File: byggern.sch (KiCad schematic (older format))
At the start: 15 parts, among them U1 ATmega162-16PU

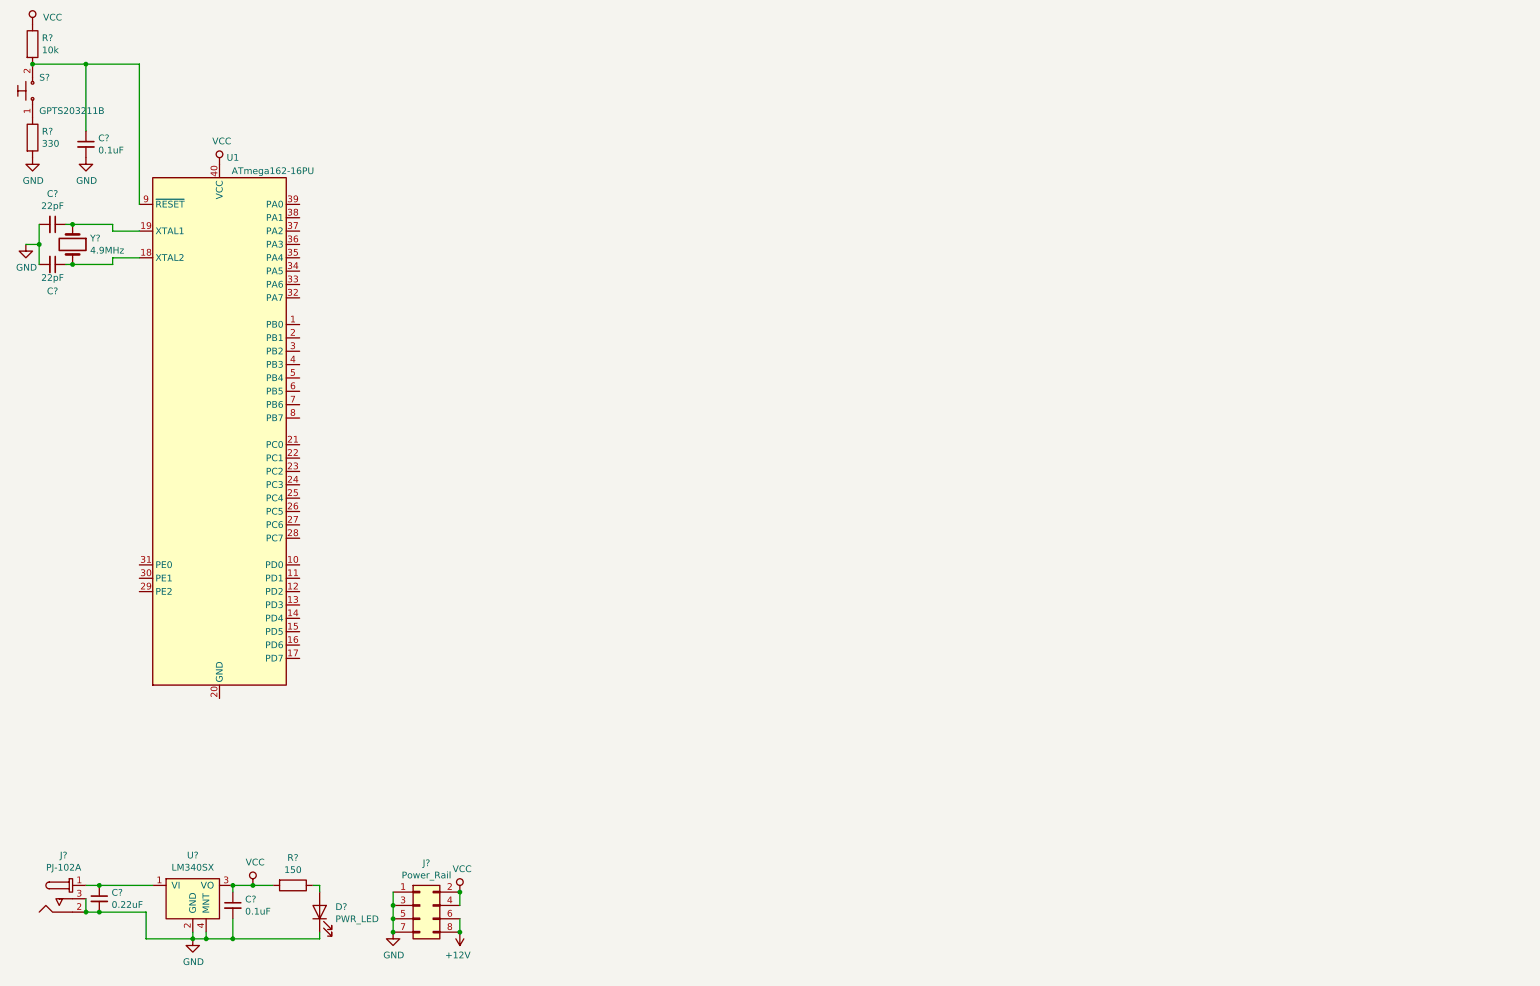
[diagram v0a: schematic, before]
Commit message: Update schematic with usart interface
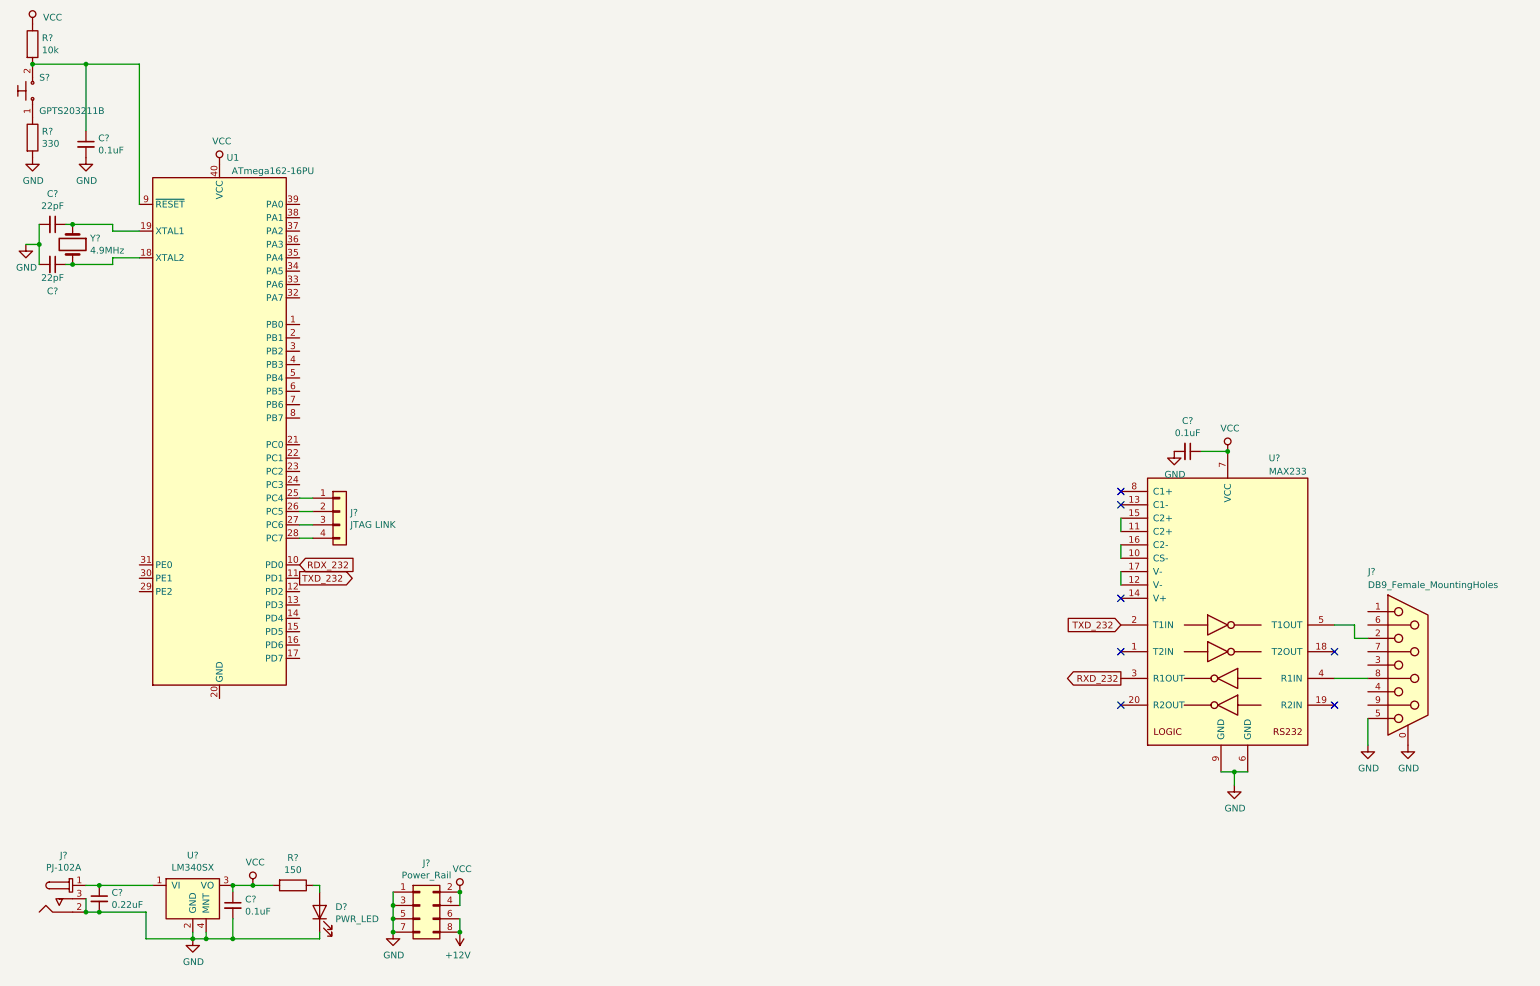
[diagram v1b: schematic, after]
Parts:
- added C?: 0.1uF, symbol Device:C_Small
- added J?: JTAG LINK, symbol Connector_Generic:Conn_01x04
- added J?: DB9_Female_MountingHoles, symbol Connector:DB9_Female_MountingHoles
- added U?: MAX233, symbol byggern:MAX233
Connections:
- net GND: now also C?.2, J?.0 (PAD), J?.5, U?.6 (GND), U?.9 (GND)
- net VCC: now also C?.1, U?.7 (VCC)
- net RDX_232: now reaches U1.10 (PD0)
- net TXD_232: now reaches U1.11 (PD1)
- net TXD_232: now also U?.2 (T1IN)
- net at U1.25 (PC4): now also J?.1 (Pin_1)
- net at U1.26 (PC5): now also J?.2 (Pin_2)
- net at U1.27 (PC6): now also J?.3 (Pin_3)
- net at U1.28 (PC7): now also J?.4 (Pin_4)
- new net: U?.10 (CS-), U?.16 (C2-)
- new net: U?.11 (C2+), U?.15 (C2+)
- new net: U?.12 (V-), U?.17 (V-)
- new net: J?.8, U?.4 (R1IN)
- new net: J?.2, U?.5 (T1OUT)
- new net RXD_232: U?.3 (R1OUT)
- no-connect marks 0 -> 7
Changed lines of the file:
@@
 EESchema Schematic File Version 4
+LIBS:byggern-cache
 EELAYER 30 0
 EELAYER END
@@
 Comment4 ""
 $EndDescr
-$Comp
-L MCU_Microchip_ATmega:ATmega162-16PU U1
-U 1 1 5D9DA1AA
-P 2100 3650
-F 0 "U1" H 2200 5700 50  0000 C CNN
-F 1 "ATmega162-16PU" H 2500 5600 50  0000 C CNN
-F 2 "Package_DIP:DIP-40_W15.24mm" H 2100 3650 50  0001 C CIN
-F 3 "http://ww1.microchip.com/downloads/en/DeviceDoc/Atmel-2513-8-bit-AVR-Microntroller-ATmega162_Datasheet.pdf" H 2100 3650 50  0001 C CNN
-	1    2100 3650
-	1    0    0    -1
-$EndComp
 $Comp
 L dk_Barrel-Power-Connectors:PJ-102A J?
@@
 	1500 900  1500 1950
 Connection ~ 1100 900
+Text GLabel 2700 4650 2    50   Input ~ 0
+RDX_232
+Text GLabel 2700 4750 2    50   Output ~ 0
+TXD_232
+Wire Wire Line
+	2800 4150 2700 4150
+$Comp
+L Connector_Generic:Conn_01x04 J?
+U 1 1 5D9DEC38
+P 3000 4250
+F 0 "J?" H 3080 4242 50  0000 L CNN
+F 1 "JTAG LINK" H 3080 4151 50  0000 L CNN
+F 2 "" H 3000 4250 50  0001 C CNN
+F 3 "~" H 3000 4250 50  0001 C CNN
+	1    3000 4250
+	1    0    0    -1
+$EndComp
+$Comp
+L MCU_Microchip_ATmega:ATmega162-16PU U1
+U 1 1 5D9DA1AA
+P 2100 3650
+F 0 "U1" H 2200 5700 50  0000 C CNN
+F 1 "ATmega162-16PU" H 2500 5600 50  0000 C CNN
+F 2 "Package_DIP:DIP-40_W15.24mm" H 2100 3650 50  0001 C CIN
+F 3 "http://ww1.microchip.com/downloads/en/DeviceDoc/Atmel-2513-8-bit-AVR-Microntroller-ATmega162_Datasheet.pdf" H 2100 3650 50  0001 C CNN
+	1    2100 3650
+	1    0    0    -1
+$EndComp
+Wire Wire Line
+	2800 4250 2700 4250
+Wire Wire Line
+	2800 4350 2700 4350
+Wire Wire Line
+	2800 4450 2700 4450
+$Comp
+L byggern:MAX233 U?
+U 1 1 5D9E4780
+P 9550 3650
+F 0 "U?" H 10000 3450 50  0000 C CNN
+F 1 "MAX233" H 10100 3350 50  0000 C CNN
+F 2 "" H 9300 3450 50  0001 C CNN
+F 3 "" H 9300 3450 50  0001 C CNN
+	1    9550 3650
+	1    0    0    -1
+$EndComp
+NoConn ~ 8850 4100
+NoConn ~ 8850 4200
+Wire Wire Line
+	8850 4300 8850 4400
+Wire Wire Line
+	8850 4500 8850 4600
+Wire Wire Line
+	8850 4700 8850 4800
+NoConn ~ 8850 4900
+Text GLabel 8850 5100 0    50   Input ~ 0
+TXD_232
+Text GLabel 8850 5500 0    50   Output ~ 0
+RXD_232
+NoConn ~ 8850 5300
+NoConn ~ 8850 5700
+NoConn ~ 10450 5300
+NoConn ~ 10450 5700
+$Comp
+L Connector:DB9_Female_MountingHoles J?
+U 1 1 5D9EEA2F
+P 11000 5400
+F 0 "J?" H 10700 6100 50  0000 L CNN
+F 1 "DB9_Female_MountingHoles" H 10700 6000 50  0000 L CNN
+F 2 "" H 11000 5400 50  0001 C CNN
+F 3 " ~" H 11000 5400 50  0001 C CNN
+	1    11000 5400
+	1    0    0    -1
+$EndComp
+Wire Wire Line
+	10450 5100 10600 5100
+Wire Wire Line
+	10600 5100 10600 5200
+Wire Wire Line
+	10600 5200 10700 5200
+Wire Wire Line
+	10450 5500 10700 5500
+$Comp
+L power:GND #PWR?
+U 1 1 5D9F4210
+P 10700 6000
+F 0 "#PWR?" H 10700 5750 50  0001 C CNN
+F 1 "GND" H 10705 5827 50  0000 C CNN
+F 2 "" H 10700 6000 50  0001 C CNN
+F 3 "" H 10700 6000 50  0001 C CNN
+	1    10700 6000
+	1    0    0    -1
+$EndComp
+$Comp
+L power:GND #PWR?
+U 1 1 5D9F4B68
+P 11000 6000
+F 0 "#PWR?" H 11000 5750 50  0001 C CNN
+F 1 "GND" H 11005 5827 50  0000 C CNN
+F 2 "" H 11000 6000 50  0001 C CNN
+F 3 "" H 11000 6000 50  0001 C CNN
+	1    11000 6000
+	1    0    0    -1
+$EndComp
+Wire Wire Line
+	10700 5800 10700 6000
+Wire Wire Line
+	9800 6200 9700 6200
+Wire Wire Line
+	9700 6200 9700 6300
+Connection ~ 9700 6200
+Wire Wire Line
+	9700 6200 9600 6200
+$Comp
+L power:GND #PWR?
+U 1 1 5DA02D2F
+P 9700 6300
+F 0 "#PWR?" H 9700 6050 50  0001 C CNN
+F 1 "GND" H 9705 6127 50  0000 C CNN
+F 2 "" H 9700 6300 50  0001 C CNN
+F 3 "" H 9700 6300 50  0001 C CNN
+	1    9700 6300
+	1    0    0    -1
+$EndComp
+$Comp
+L Device:C_Small C?
+U 1 1 5DA03DBF
+P 9350 3800
+F 0 "C?" V 9121 3800 50  0000 C CNN
+F 1 "0.1uF" V 9212 3800 50  0000 C CNN
+F 2 "" H 9350 3800 50  0001 C CNN
+F 3 "~" H 9350 3800 50  0001 C CNN
+	1    9350 3800
+	0    1    1    0
+$EndComp
+$Comp
+L power:VCC #PWR?
+U 1 1 5D9E6B36
+P 9650 3800
+F 0 "#PWR?" H 9650 3650 50  0001 C CNN
+F 1 "VCC" H 9667 3973 50  0000 C CNN
+F 2 "" H 9650 3800 50  0001 C CNN
+F 3 "" H 9650 3800 50  0001 C CNN
+	1    9650 3800
+	1    0    0    -1
+$EndComp
+Wire Wire Line
+	9450 3800 9650 3800
+Connection ~ 9650 3800
+$Comp
+L power:GND #PWR?
+U 1 1 5DA0B668
+P 9250 3800
+F 0 "#PWR?" H 9250 3550 50  0001 C CNN
+F 1 "GND" H 9255 3627 50  0000 C CNN
+F 2 "" H 9250 3800 50  0001 C CNN
+F 3 "" H 9250 3800 50  0001 C CNN
+	1    9250 3800
+	1    0    0    -1
+$EndComp
 $EndSCHEMATC

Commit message: Complete schematic, quality check remaining
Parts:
- added C? (x6): 0.1uF, symbol Device:C_Small
- added C?: C_Small, symbol Device:C_Small
- added C? (x2): 22pF, symbol Device:C_Small
- added J?: OLED_Connection, symbol Connector_Generic:Conn_01x12
- added J?: Joystick_Slider_buttons_connector, symbol Connector_Generic:Conn_01x06
- added J?: CAN, symbol Connector_Generic:Conn_01x02
- added R?: 22K, symbol Device:R
- added R? (x2): 120, symbol Device:R_Small
- added U?: GAL16V8, symbol Logic_Programmable:GAL16V8
- added U?: SN74ALS573CN, symbol byggern:SN74ALS573CN
- added U?: IDT7164, symbol byggern:IDT7164
- added U?: ADC0844, symbol byggern:ADC0844
- added U?: MCP2515, symbol byggern:MCP2515
- added U?: MCP2551, symbol byggern:MCP2551
- added Y?: 16MHz, symbol Device:Crystal
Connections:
- net RDX_232 is gone; now on net RXD_232: U1.10 (PD0)
- net GND: now also U1.20 (GND), C?.2, C?.2, C?.2, C?.2, C?.2, C?.2, C?.2, C?.2, J?.12 (Pin_12), R?.2, U?.1 (~OE), U?.10 (DGND), U?.10 (GND), U?.10 (GND), U?.14 (GND), U?.2 (A12), U?.2 (VSS), U?.7 (AGND)
- net VCC: now also C?.1, C?.1, C?.1, C?.1, C?.1, C?.1, C?.1, U?.18 (VDD), U?.20 (VCC), U?.20 (VCC), U?.20 (VCC), U?.26 (CS2), U?.28 (Vcc), U?.3 (VDD), U?.8 (VREF)
- net SOUND_PWM: now reaches U1.1 (PB0)
- net CAN_~INT~: now reaches U1.12 (PD2)
- net CAN_~INT~: now also U?.12 (~INT)
- net ~WR~: now reaches U1.16 (PD6)
- net ~WR~: now also J?.3 (Pin_3), U?.19 (~WR), U?.27 (~WE)
- net ~OE~: now reaches U1.17 (PD7)
- net ~OE~: now also U?.1 (~RD), U?.22 (~OE)
- net BUTTON_LEFT: now reaches U1.2 (PB1)
- net BUTTON_LEFT: now also J?.5 (Pin_5)
- net A8: now reaches U1.21 (PC0)
- net A8: now also U?.1 (I1/CLK), U?.25 (A8)
- net A9: now reaches U1.22 (PC1)
- net A9: now also U?.2 (I2), U?.24 (A9)
- net A10: now reaches U1.23 (PC2)
- net A10: now also U?.21 (A10), U?.3 (I3)
- net A11: now reaches U1.24 (PC3)
- net A11: now also U?.23 (A11), U?.4 (I4)
- net BUTTON_RIGHT: now reaches U1.3 (PB2)
- net BUTTON_RIGHT: now also J?.6 (Pin_6)
- net LE: now reaches U1.30 (PE1)
- net LE: now also U?.11 (LE)
- net A7: now reaches U1.32 (PA7)
- net A7: now also J?.11 (Pin_11), U?.19 (IO/7), U?.9 (8D), U?.9 (DB7)
- net A6: now reaches U1.33 (PA6)
- net A6: now also J?.10 (Pin_10), U?.11 (BD6), U?.18 (IO/6), U?.8 (7D)
- net A5: now reaches U1.34 (PA5)
- net A5: now also J?.9 (Pin_9), U?.12 (DB5), U?.17 (I/O5), U?.7 (6D)
- net A4: now reaches U1.35 (PA4)
- net A4: now also J?.8 (Pin_8), U?.13 (DB4), U?.16 (I/O4), U?.6 (5D)
- net A3: now reaches U1.36 (PA3)
- net A3: now also J?.7 (Pin_7), U?.14 (DB3), U?.15 (I/O3), U?.5 (4D)
- net A2: now reaches U1.37 (PA2)
- net A2: now also J?.6 (Pin_6), U?.13 (I/O2), U?.15 (DB2), U?.4 (3D)
- net A1: now reaches U1.38 (PA1)
- net A1: now also J?.5 (Pin_5), U?.12 (I/O1), U?.16 (DB1), U?.3 (2D)
- net A0: now reaches U1.39 (PA0)
- net A0: now also J?.4 (Pin_4), U?.11 (I/O0), U?.17 (DB0), U?.2 (1D)
- net ~CS~_MCP: now reaches U1.5 (PB4)
- net ~CS~_MCP: now also U?.16 (~CS)
- net MOSI: now reaches U1.6 (PB5)
- net MOSI: now also U?.14 (SI)
- net MISO: now reaches U1.7 (PB6)
- net MISO: now also U?.15 (SO)
- net SCK: now reaches U1.8 (PB7)
- net SCK: now also U?.13 (SCK)
- net ~RESET~: now reaches C?.1, R?.2, S?.2, U1.9 (~RESET)
- net ~RESET~: now also U?.17 (~RESET)
- new net: U?.1 (TXCAN), U?.1 (TXD)
- new net: U?.2 (RXCAN), U?.4 (RXD)
- new net: C?.1, U?.7 (OSC2), Y?.2
- new net: C?.1, U?.8 (OSC1), Y?.1
- new net: J?.2 (Pin_2), R?.2, R?.2, U?.6 (CANL)
- new net: J?.1 (Pin_1), R?.1, R?.1, U?.7 (CANH)
- new net: R?.1, U?.8 (Rs)
- new net ADC_CH1: J?.1 (Pin_1), U?.3 (CH1)
- new net ADC_CH2: J?.2 (Pin_2), U?.4 (CH2)
- new net ADC_CH3: J?.3 (Pin_3), U?.5 (CH3)
- new net ADC_CH4: J?.4 (Pin_4), U?.6 (CH4)
- new net AL0: U?.10 (A0), U?.19 (1Q)
- new net AL1: U?.18 (2Q), U?.9 (A1)
- new net AL2: U?.17 (3Q), U?.8 (A2)
- new net AL3: U?.16 (4Q), U?.7 (A3)
- new net AL4: U?.15 (5Q), U?.6 (A4)
- new net AL5: U?.14 (6Q), U?.5 (A5)
- new net AL6: U?.13 (7Q), U?.4 (A6)
- new net AL7: U?.12 (8Q), U?.3 (A7)
- new net ~CS~_ADC: U?.18 (IO2), U?.2 (~CS~)
- new net ~CS~_OLED: J?.1 (Pin_1), U?.17 (I03)
- new net ~CS~_RAM: U?.19 (IO1), U?.20 (~CS~1)
- new net ~D~\C: J?.2 (Pin_2), U?.16 (IO4)
- no-connect marks 7 -> 32
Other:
- note added: "8 bit data bus and\nlower 8 bits of 13 bit address bus"
- moved on the sheet: J?
